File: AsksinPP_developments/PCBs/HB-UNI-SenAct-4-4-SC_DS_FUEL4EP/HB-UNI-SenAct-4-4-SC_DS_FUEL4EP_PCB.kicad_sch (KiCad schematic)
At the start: 53 parts, among them J1 5V supply, J10 charge, J2 4x Push Buttons, J3 4x Relais, J4 5x LEDs, J5 ISP Programmer, J6 Accumulator, J7 GND, J8 VCC, Q1 IRLU024N, Q2 BD238, Q4 IRF9Z34N, Q5 MCP1702-2802E_TO, SW1 SW_Push, SW2 SW_Push

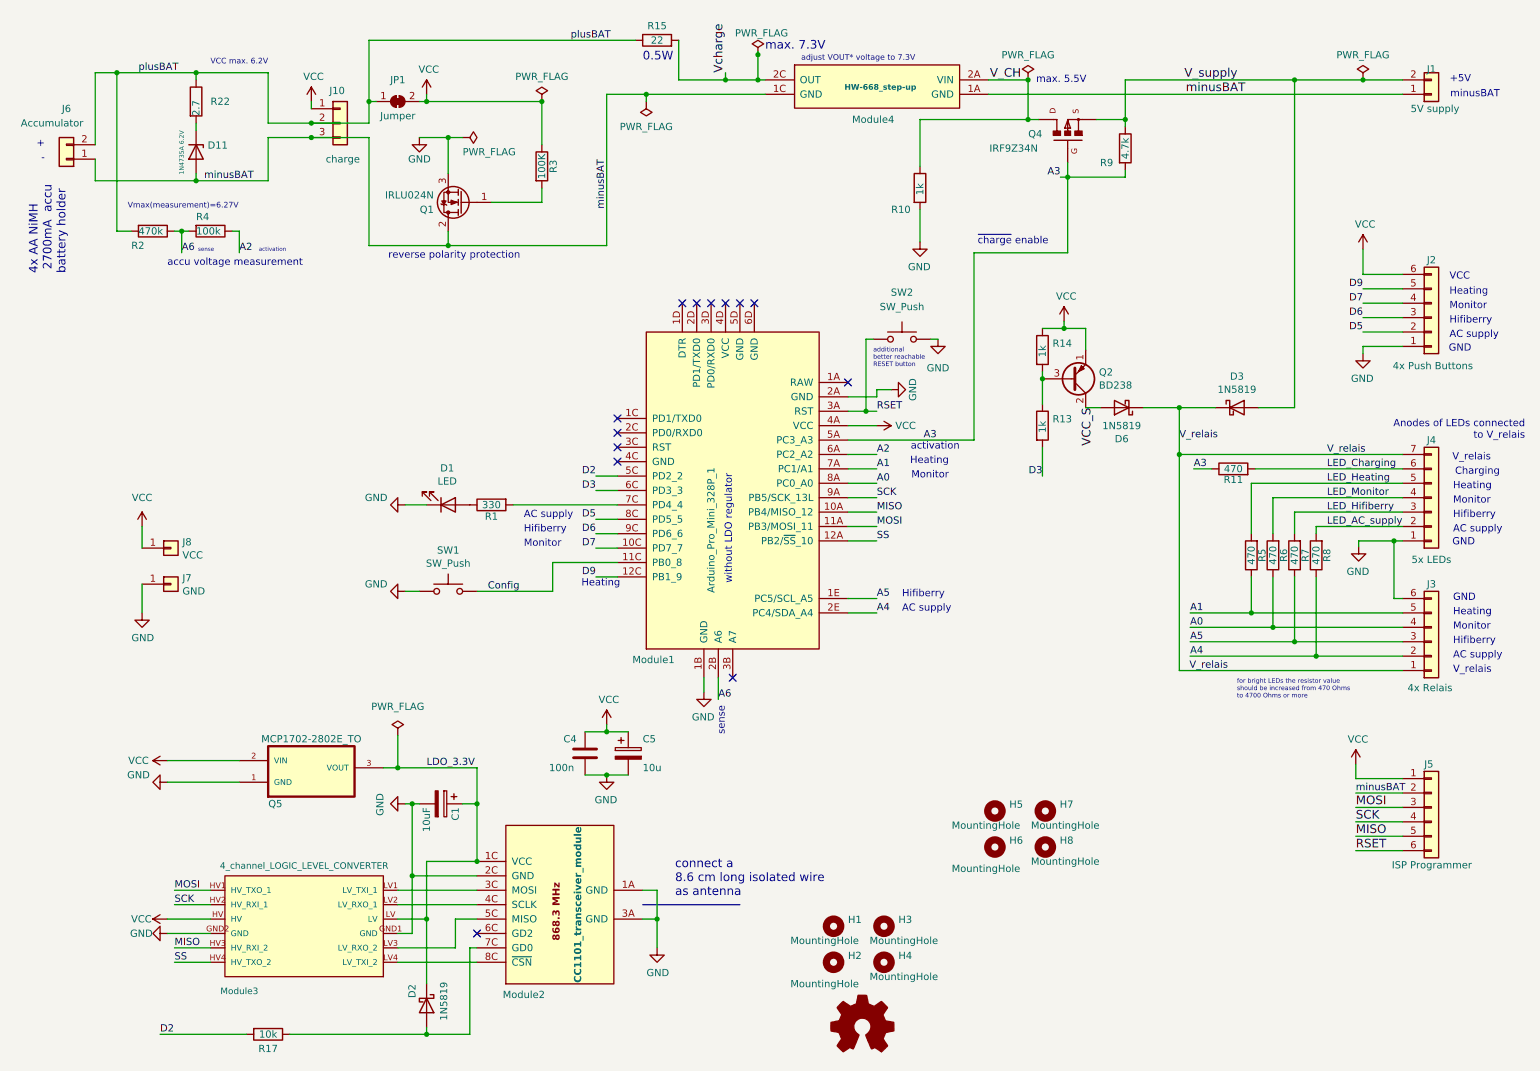
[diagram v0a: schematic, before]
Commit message: PCBs: KiCAD6 required improvements of layout data bases; added E07-900M10S into FUEL and footprint library
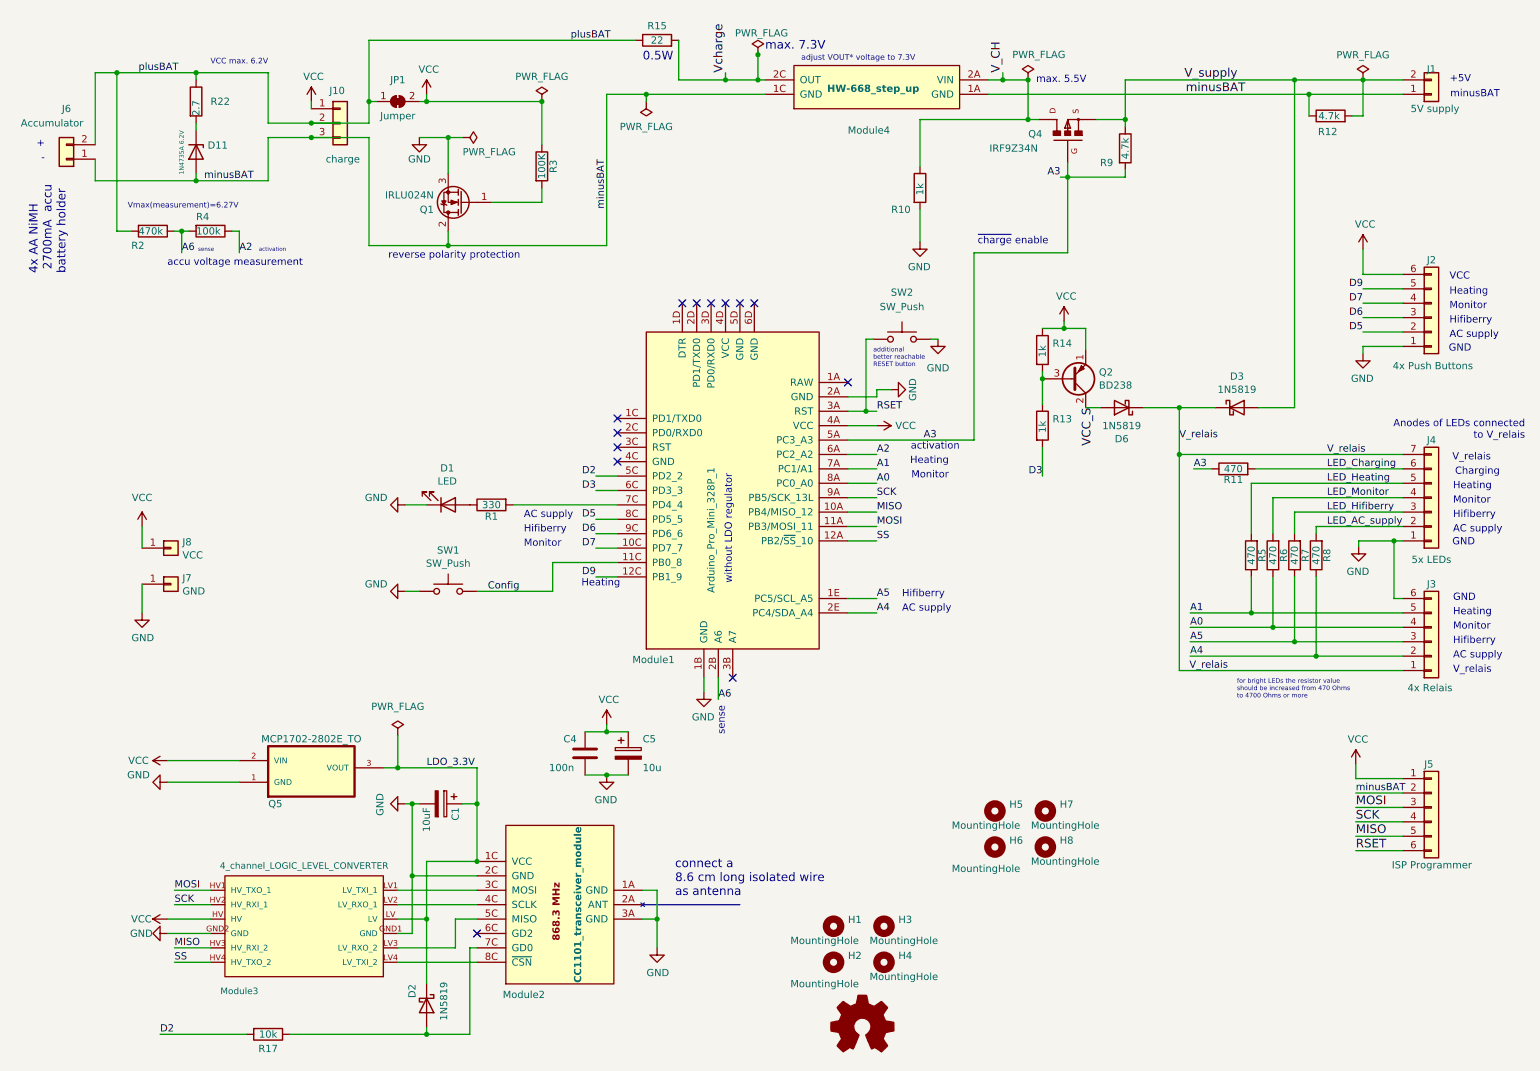
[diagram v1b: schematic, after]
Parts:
- removed Module4: HW-668_step-up, FUEL4EP:HW-668_step-up, symbol FUEL4EP:HW-668_step-up
- added Module4: HW-668_step_up, FUEL4EP:HW-668_step-up, symbol FUEL4EP:HW-668_step_up
- added R12: 4.7k, Resistor_THT:R_Axial_DIN0204_L3.6mm_D1.6mm_P5.08mm_Horizontal, symbol Device:R
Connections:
- net V_CH: now also Module4.2A (VIN)
- net V_supply: now also R12.2
- net Vcharge: now also Module4.2C (OUT)
- net minusBAT: now also Module4.1A (GND), Module4.1C (GND), R12.1
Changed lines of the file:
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@@
   (title_block
     (title "SenAct-4-4-SC_FUEL4EP_PCB")
-    (date "2023-07-13")
-    (rev "1.3")
+    (date "2023-07-22")
+    (rev "1.4")
     (company "FUEL4EP")
     (comment 1 "3x Schalter Schaltaktor AsksinPP PCB für Netzfreischalter")
@@
   (junction (at 197.485 66.675) (diameter 0) (color 0 0 0 0)
   )
+  (junction (at 186.69 22.86) (diameter 0) (color 0 0 0 0)
+  )
   (junction (at 230.505 116.84) (diameter 0) (color 0 0 0 0)
   )
@@
   (junction (at 85.09 170.815) (diameter 0) (color 0 0 0 0)
   )
+  (junction (at 240.665 25.4) (diameter 0) (color 0 0 0 0)
+  )
+  (junction (at 143.51 18.415) (diameter 0) (color 0 0 0 0)
+  )
+  (junction (at 217.805 80.645) (diameter 0) (color 0 0 0 0)
+  )
+  (junction (at 125.73 170.815) (diameter 0) (color 0 0 0 0)
+  )
+  (junction (at 44.45 40.64) (diameter 0) (color 0 0 0 0)
+  )
+  (junction (at 116.84 137.795) (diameter 0) (color 0 0 0 0)
+  )
+  (junction (at 30.48 21.59) (diameter 0) (color 0 0 0 0)
+  )
+  (junction (at 238.125 121.92) (diameter 0) (color 0 0 0 0)
+  )
+  (junction (at 80.01 144.145) (diameter 0) (color 0 0 0 0)
+  )
+  (junction (at 64.77 30.48) (diameter 0) (color 0 0 0 0)
+  )
+  (junction (at 208.28 29.845) (diameter 0) (color 0 0 0 0)
+  )
+  (junction (at 82.55 150.495) (diameter 0) (color 0 0 0 0)
+  )
+  (junction (at 64.77 33.02) (diameter 0) (color 0 0 0 0)
+  )
+  (junction (at 162.56 81.28) (diameter 0) (color 0 0 0 0)
+  )
   (junction (at 191.135 22.86) (diameter 0) (color 0 0 0 0)
   )
-  (junction (at 143.51 18.415) (diameter 0) (color 0 0 0 0)
-  )
-  (junction (at 217.805 80.645) (diameter 0) (color 0 0 0 0)
-  )
-  (junction (at 125.73 170.815) (diameter 0) (color 0 0 0 0)
-  )
-  (junction (at 44.45 40.64) (diameter 0) (color 0 0 0 0)
-  )
-  (junction (at 116.84 137.795) (diameter 0) (color 0 0 0 0)
-  )
-  (junction (at 30.48 21.59) (diameter 0) (color 0 0 0 0)
-  )
-  (junction (at 238.125 121.92) (diameter 0) (color 0 0 0 0)
-  )
-  (junction (at 80.01 144.145) (diameter 0) (color 0 0 0 0)
-  )
-  (junction (at 64.77 30.48) (diameter 0) (color 0 0 0 0)
-  )
-  (junction (at 208.28 29.845) (diameter 0) (color 0 0 0 0)
-  )
-  (junction (at 82.55 150.495) (diameter 0) (color 0 0 0 0)
-  )
-  (junction (at 64.77 33.02) (diameter 0) (color 0 0 0 0)
-  )
-  (junction (at 162.56 81.28) (diameter 0) (color 0 0 0 0)
-  )
   (junction (at 238.125 22.86) (diameter 0) (color 0 0 0 0)
   )
   (junction (at 193.675 75.565) (diameter 0) (color 0 0 0 0)
   )
+  (junction (at 88.9 52.07) (diameter 0) (color 0 0 0 0)
+  )
+  (junction (at 93.98 150.495) (diameter 0) (color 0 0 0 0)
+  )
+  (junction (at 198.12 40.005) (diameter 0) (color 0 0 0 0)
+  )
+  (junction (at 44.45 21.59) (diameter 0) (color 0 0 0 0)
+  )
   (junction (at 191.135 29.845) (diameter 0) (color 0 0 0 0)
-  )
-  (junction (at 88.9 52.07) (diameter 0) (color 0 0 0 0)
-  )
-  (junction (at 93.98 150.495) (diameter 0) (color 0 0 0 0)
-  )
-  (junction (at 198.12 40.005) (diameter 0) (color 0 0 0 0)
-  )
-  (junction (at 44.45 21.59) (diameter 0) (color 0 0 0 0)
   )
   (junction (at 217.805 88.9) (diameter 0) (color 0 0 0 0)
@@
     (stroke (width 0) (type default) (color 0 0 0 0))
   )
-  (wire (pts (xy 193.04 29.845) (xy 191.135 29.845))
+  (wire (pts (xy 172.085 29.845) (xy 191.135 29.845))
     (stroke (width 0) (type default) (color 0 0 0 0))
   )
@@
     (stroke (width 0) (type default) (color 0 0 0 0))
   )
-  (wire (pts (xy 191.135 29.845) (xy 172.085 29.845))
+  (wire (pts (xy 191.135 29.845) (xy 193.04 29.845))
     (stroke (width 0) (type default) (color 0 0 0 0))
   )
@@
     (stroke (width 0) (type default) (color 0 0 0 0))
   )
+  (wire (pts (xy 184.15 25.4) (xy 240.665 25.4))
+    (stroke (width 0) (type default) (color 0 0 0 0))
+  )
   (wire (pts (xy 85.09 160.655) (xy 93.98 160.655))
     (stroke (width 0) (type default) (color 0 0 0 0))
@@
     (stroke (width 0) (type default) (color 0 0 0 0))
   )
+  (wire (pts (xy 250.19 29.21) (xy 248.285 29.21))
+    (stroke (width 0) (type default) (color 0 0 0 0))
+  )
   (wire (pts (xy 159.385 101.6) (xy 164.465 101.6))
     (stroke (width 0) (type default) (color 0 0 0 0))
@@
     (stroke (width 0) (type default) (color 0 0 0 0))
   )
+  (wire (pts (xy 240.665 25.4) (xy 257.175 25.4))
+    (stroke (width 0) (type default) (color 0 0 0 0))
+  )
   (wire (pts (xy 118.745 110.49) (xy 114.935 110.49))
     (stroke (width 0) (type default) (color 0 0 0 0))
   )
+  (wire (pts (xy 191.135 22.86) (xy 191.135 29.845))
+    (stroke (width 0) (type default) (color 0 0 0 0))
+  )
   (wire (pts (xy 136.525 128.27) (xy 136.525 132.08))
     (stroke (width 0) (type default) (color 0 0 0 0))
@@
     (stroke (width 0) (type default) (color 0 0 0 0))
   )
-  (wire (pts (xy 191.135 22.86) (xy 184.15 22.86))
-    (stroke (width 0) (type default) (color 0 0 0 0))
-  )
   (wire (pts (xy 44.45 30.48) (xy 44.45 31.75))
     (stroke (width 0) (type default) (color 0 0 0 0))
@@
     (stroke (width 0) (type default) (color 0 0 0 0))
   )
-  (wire (pts (xy 184.15 25.4) (xy 257.175 25.4))
-    (stroke (width 0) (type default) (color 0 0 0 0))
-  )
   (wire (pts (xy 123.19 170.815) (xy 125.73 170.815))
     (stroke (width 0) (type default) (color 0 0 0 0))
@@
     (stroke (width 0) (type default) (color 0 0 0 0))
   )
+  (wire (pts (xy 250.19 22.86) (xy 250.19 29.21))
+    (stroke (width 0) (type default) (color 0 0 0 0))
+  )
   (wire (pts (xy 123.19 165.735) (xy 125.73 165.735))
     (stroke (width 0) (type default) (color 0 0 0 0))
@@
     (stroke (width 0) (type default) (color 0 0 0 0))
   )
+  (wire (pts (xy 240.665 25.4) (xy 240.665 29.21))
+    (stroke (width 0) (type default) (color 0 0 0 0))
+  )
   (wire (pts (xy 90.17 170.815) (xy 90.17 175.895))
     (stroke (width 0) (type default) (color 0 0 0 0))
@@
     (stroke (width 0) (type default) (color 0 0 0 0))
   )
+  (wire (pts (xy 186.69 21.59) (xy 186.69 22.86))
+    (stroke (width 0) (type default) (color 0 0 0 0))
+  )
   (wire (pts (xy 198.12 37.465) (xy 198.12 40.005))
     (stroke (width 0) (type default) (color 0 0 0 0))
@@
     (stroke (width 0) (type default) (color 0 0 0 0))
   )
+  (wire (pts (xy 184.15 22.86) (xy 186.69 22.86))
+    (stroke (width 0) (type default) (color 0 0 0 0))
+  )
+  (wire (pts (xy 186.69 22.86) (xy 191.135 22.86))
+    (stroke (width 0) (type default) (color 0 0 0 0))
+  )
   (wire (pts (xy 85.09 160.655) (xy 85.09 170.815))
     (stroke (width 0) (type default) (color 0 0 0 0))
@@
   )
   (wire (pts (xy 82.55 163.195) (xy 82.55 150.495))
-    (stroke (width 0) (type default) (color 0 0 0 0))
-  )
-  (wire (pts (xy 191.135 29.845) (xy 191.135 22.86))
     (stroke (width 0) (type default) (color 0 0 0 0))
   )
@@
     (effects (font (size 1.27 1.27)) (justify right bottom))
   )
-  (label "V_CH" (at 184.404 22.86 0)
+  (label "V_CH" (at 186.69 21.59 90)
     (effects (font (size 1.524 1.524)) (justify left bottom))
   )
@@
       (effects (font (size 1.27 1.27)) hide)
     )
-    (property "Value" "PWR_FLAG" (id 1) (at 191.135 18.4658 0))
+    (property "Value" "PWR_FLAG" (id 1) (at 193.04 18.415 0))
     (property "Footprint" "" (id 2) (at 191.135 22.86 0)
       (effects (font (size 1.27 1.27)) hide)
@@
     (pin "2")
   )
-  (symbol (lib_id "FUEL4EP:HW-668_step-up") (at 149.86 27.94 0) (mirror x) (unit 1)
-    (in_bom yes) (on_board yes)
-    (property "Reference" "Module4" (id 0) (at 163.83 29.845 0))
-    (property "Value" "HW-668_step-up" (id 1) (at 165.1 24.13 0)
-      (effects (font (size 1 1) bold))
-    )
-    (property "Footprint" "FUEL4EP:HW-668_step-up" (id 2) (at 153.7716 17.6784 0)
-      (effects (font (size 1.27 1.27)) hide)
-    )
-    (property "Datasheet" "https://datasheet.lcsc.com/szlcsc/Shenzhen-Suosemi-Tech-SX1308_C78162.pdf" (id 3) (at 173.99 12.7 0)
+  (symbol (lib_id "FUEL4EP:HW-668_step_up") (at 175.26 27.94 0) (mirror x) (unit 1)
+    (in_bom yes) (on_board yes)
+    (property "Reference" "Module4" (id 0) (at 163.068 31.75 0))
+    (property "Value" "HW-668_step_up" (id 1) (at 163.83 24.384 0)
+      (effects (font (size 1.27 1.27) bold))
+    )
+    (property "Footprint" "FUEL4EP:HW-668_step-up" (id 2) (at 153.67 17.78 0)
+      (effects (font (size 1.27 1.27)) hide)
+    )
+    (property "Datasheet" "https://datasheetspdf.com/pdf-file/921054/Suosemi/SX1308/1" (id 3) (at 167.64 14.605 0)
       (effects (font (size 1.27 1.27)) hide)
     )
@@
     (pin "2A")
     (pin "2C")
+  )
+  (symbol (lib_id "Device:R") (at 244.475 29.21 90) (unit 1)
+    (in_bom yes) (on_board yes)
+    (property "Reference" "R12" (id 0) (at 243.967 32.004 90))
+    (property "Value" "4.7k" (id 1) (at 244.221 29.21 90))
+    (property "Footprint" "Resistor_THT:R_Axial_DIN0204_L3.6mm_D1.6mm_P5.08mm_Horizontal" (id 2) (at 244.475 30.988 90)
+      (effects (font (size 1.27 1.27)) hide)
+    )
+    (property "Datasheet" "~" (id 3) (at 244.475 29.21 0)
+      (effects (font (size 1.27 1.27)) hide)
+    )
+    (pin "1")
+    (pin "2")
   )
   (symbol (lib_id "Switch:SW_Push") (at 168.91 68.58 0) (unit 1)
@@
       (reference "Module3") (unit 1) (value "4_channel_LOGIC_LEVEL_CONVERTER") (footprint "FUEL4EP:4_channel_LOGIC_LEVEL_CONVERTER")
     )
-    (path "/77dbf059-fbca-4af7-9d32-aeed2db5bf69"
-      (reference "Module4") (unit 1) (value "HW-668_step-up") (footprint "FUEL4EP:HW-668_step-up")
+    (path "/8b764394-f7a5-407a-ad66-c1415d7815e6"
+      (reference "Module4") (unit 1) (value "HW-668_step_up") (footprint "FUEL4EP:HW-668_step-up")
     )
     (path "/00000000-0000-0000-0000-00005ae8d841"
@@
       (reference "R11") (unit 1) (value "470") (footprint "Resistor_THT:R_Axial_DIN0204_L3.6mm_D1.6mm_P5.08mm_Horizontal")
     )
+    (path "/a2a4bcff-26d0-48c1-8ae3-4d58ad966d77"
+      (reference "R12") (unit 1) (value "4.7k") (footprint "Resistor_THT:R_Axial_DIN0204_L3.6mm_D1.6mm_P5.08mm_Horizontal")
+    )
     (path "/00000000-0000-0000-0000-00006177e8b3"
